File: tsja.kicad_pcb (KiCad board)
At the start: 4 copper layers, 95 x 86 mm, 114 parts, among them J1 QWIIC, J10 E-Paper, J2 Micro_SD_Card, J3 SAO, J4 EXT, J6 USB-C, J9 Battery, M1 Vibration, Q1 AP2302B, Q2 AP2302B, Q3 AP2302B, Q4 AO3400 (A09T), Q5 AO3400 (A09T), SW6 SW_SPDT, T1 Select, T2 Start, T3 B, T4 A, T5 Cross, U1 74LVC1G17GW,125, U10 SY6280AAC, U11 SK6805, U12 SK6805, U13 SK6805, U14 SK6805, U15 SK6805, U2 MPR121QR2, U3 ESP32-WROVER-E, U4 SY8079AAC, U5 XT4054K421MR-G, U6 SY6280AAC, U7 CH340K, U8 SK6805, U9 SY6280AAC

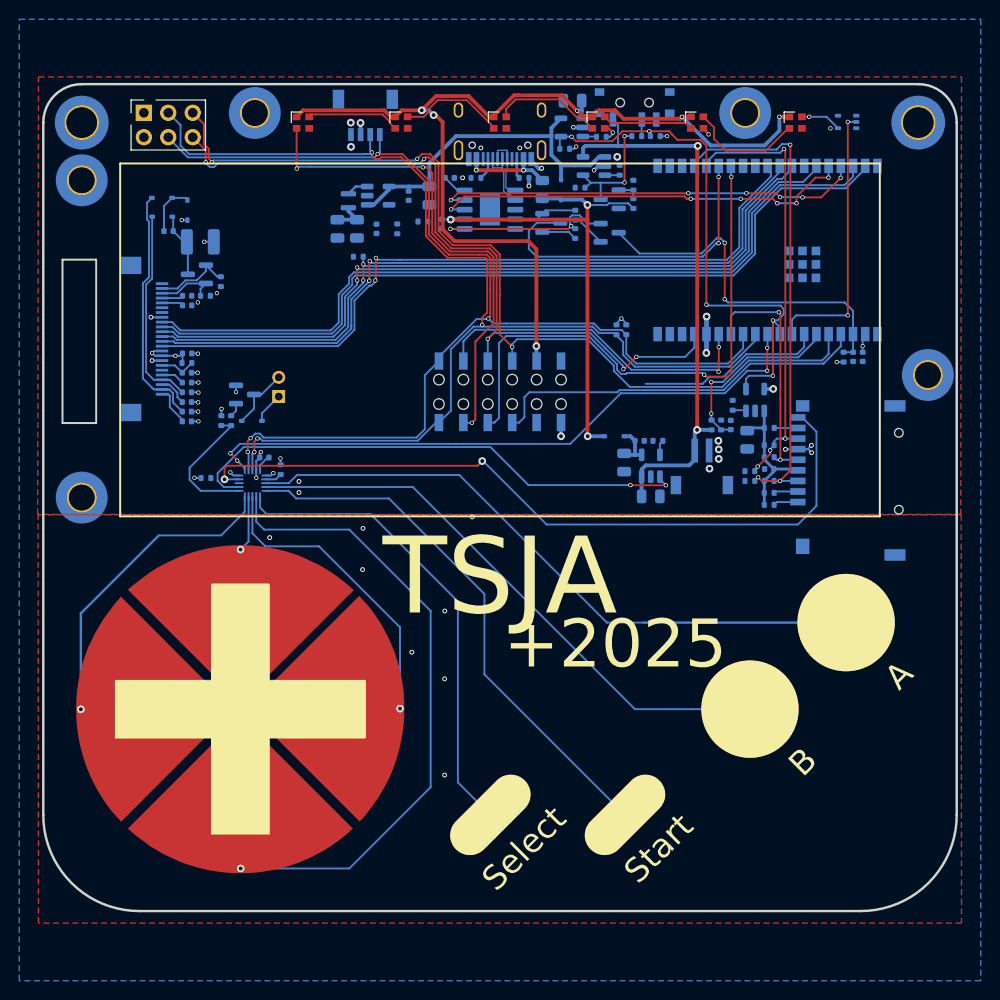
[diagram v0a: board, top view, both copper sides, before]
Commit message: Use DC/DC from WHY badge
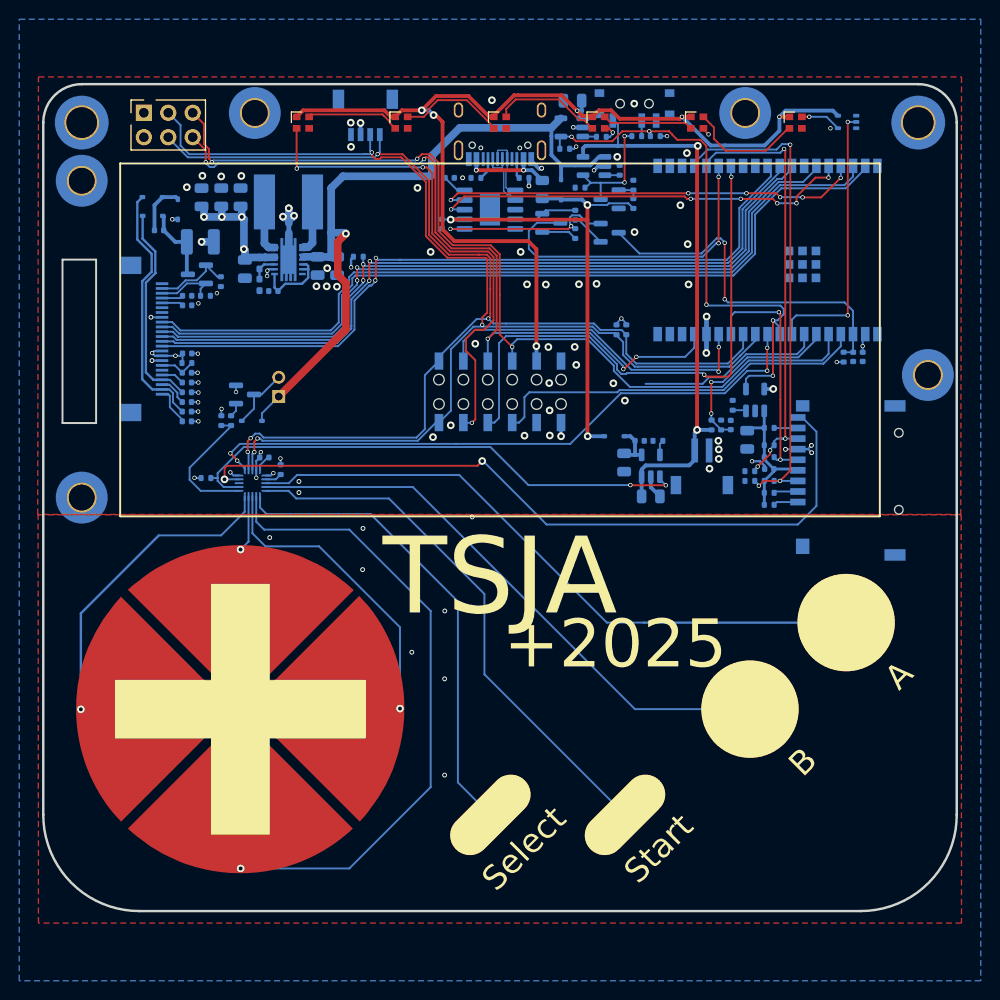
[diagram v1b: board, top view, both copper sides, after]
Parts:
- removed R23: 10k, Resistor_SMD:R_0402_1005Metric
- removed R24: 45.3k, Resistor_SMD:R_0402_1005Metric
- added C28: 10u, Capacitor_SMD:C_0805_2012Metric, B.Cu at (-19.0, -24.3)
- added C29: 100n, Capacitor_SMD:C_0402_1005Metric, B.Cu at (-23.6, -21.7)
- added JP1: ~, NetTie:NetTie-2_SMD_Pad0.5mm, B.Cu at (-22.0, -28.3)
- added R11: 1M, Resistor_SMD:R_0402_1005Metric_Pad0.72x0.64mm_HandSolder, B.Cu at (-25.0, -24.6)
- added R12: 180k, Resistor_SMD:R_0402_1005Metric_Pad0.72x0.64mm_HandSolder, B.Cu at (-25.0, -22.4)
- C10: value 22u -> 10u
- C4: value 100n -> 22u; footprint Capacitor_SMD:C_0402_1005Metric -> Capacitor_SMD:C_0805_2012Metric
- C7: value 22p -> 22u; footprint Capacitor_SMD:C_0402_1005Metric -> Capacitor_SMD:C_0805_2012Metric
- L1: value 2.2u -> CMLW6028S1R5MST; footprint library:Inductor_MSC20FC -> library:IND-SMD_L6.0-W6.0
- U4: value SY8079AAC -> TPS63020DSJR; footprint library:SOT-23-5 -> library:VSON-14_L4.0-W3.0-P0.50-BL-EP_TI_DSJ
- moved C5 19.6 mm to (-27.0, -31.5), turned to 90 degrees
- moved C4 18.7 mm to (-26.5, -24.0)
- moved C9 16.5 mm to (-31.0, -31.5), turned to 90 degrees
- moved C7 16.5 mm to (-29.0, -31.5)
- moved U4 11.5 mm to (-22.0, -25.0), turned to 90 degrees
- moved L1 6.24 mm to (-22.0, -31.0), turned to 0 degrees
- moved C10 3.87 mm to (-16.9, -24.3)
- moved C13 0.99 mm to (-35.5, -28.0)
- moved D25 0.99 mm to (-33.5, -30.2)
- moved D26 0.99 mm to (-36.1, -31.5)
- moved D27 0.99 mm to (-36.1, -29.5)
- moved SW6 0.11 mm to (14.0, -40.9)
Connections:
- C10 pad 1: +3.3V -> VIN
- C4 pad 1: VIN -> +3.3V
- C5 pad 1: VIN -> +3.3V
- C7 pad 2: /Power management/FB33 -> GND
- L1 pad 1: +3.3V -> Net-(L1-Pad1)
- L1 pad 2: /Power management/SW33 -> Net-(L1-Pad2)
- U4 pad 1: VIN -> Net-(U4-EN)
- U4 pad 3: /Power management/SW33 -> Net-(U4-FB)
- U4 pad 4: VIN -> +3.3V
- U4 pad 5: /Power management/FB33 -> +3.3V
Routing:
- net VIN: track 39.1 -> 74.9 mm, vias 0 -> 1
- net +3.3V: track 19.9 -> 32.9 mm, vias 11 -> 16
- net GND: track 30.7 -> 39.2 mm, vias 52 -> 92
- net Net-(U4-EN): track 0.00 -> 8.12 mm
- net VLED: track 99.0 -> 105.5 mm
- net Net-(L1-Pad1): track 0.00 -> 5.57 mm
- net Net-(L1-Pad2): track 0.00 -> 5.45 mm
- net Net-(U4-FB): track 0.00 -> 2.81 mm
- net GNDPWR: track 0.00 -> 2.79 mm
- net /Power management/SW33: track 2.27 -> 0.00 mm
- net LED_OUT: track 51.5 -> 52.8 mm
- net Net-(D27-A): track 6.84 -> 8.01 mm
- net /E-Paper/PREVGL: track 25.4 -> 26.3 mm
- net /E-Paper/PREVGH: track 21.1 -> 21.9 mm
- net CHRG: track 53.8 -> 54.5 mm

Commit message: Small fixes
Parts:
- H2: footprint MountingHole:MountingHole_3.2mm_M3_DIN965_Pad_TopOnly -> MountingHole:MountingHole_3.2mm_M3_DIN965
- H5: footprint MountingHole:MountingHole_2.7mm_M2.5_Pad_TopOnly -> MountingHole:MountingHole_2.7mm_M2.5_DIN965
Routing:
- net E4: track 39.9 -> 41.8 mm
- net VBUS: track 52.4 -> 53.4 mm
- net TOUCH_INT: track 65.5 -> 66.4 mm
- net GND: vias 92 -> 97

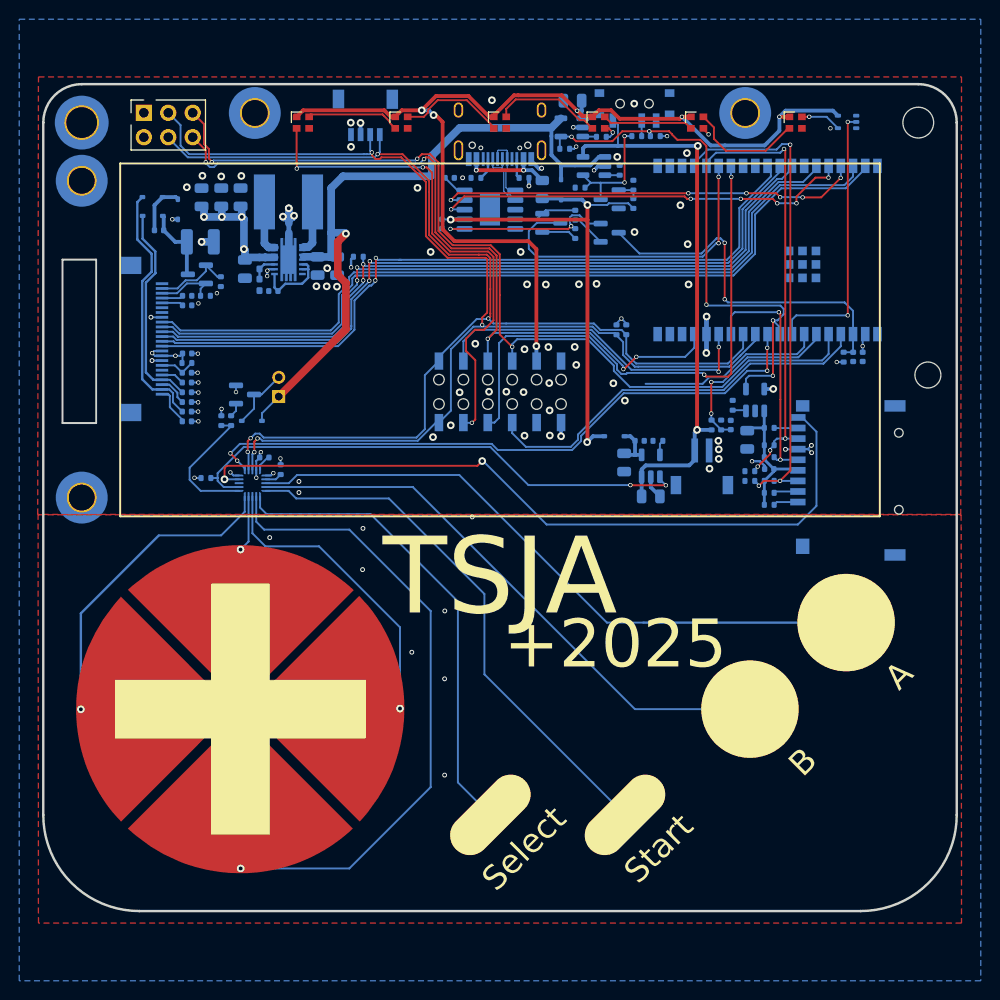
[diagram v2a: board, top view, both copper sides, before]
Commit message: Fix some routing issues, add GND vias, add capacitor for M1, add spacing between vias for ground to pour inbetween.
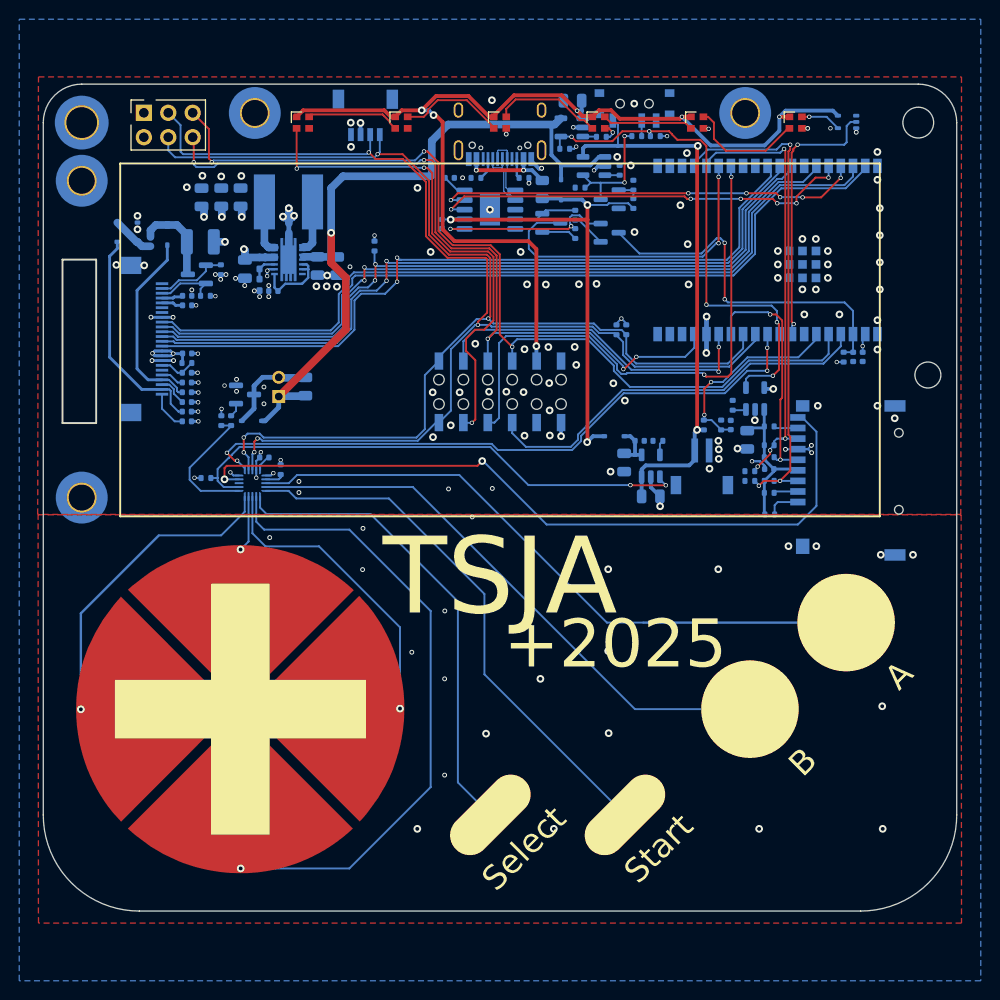
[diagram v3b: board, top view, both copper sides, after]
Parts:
- added C30: 22u, Capacitor_SMD:C_0805_2012Metric, B.Cu at (-20.2, -11.8)
- moved D25 5.43 mm to (-38.8, -28.9), turned to 180 degrees
- moved D26 5.33 mm to (-38.8, -26.9)
- moved D27 2.51 mm to (-34.6, -27.6), turned to 90 degrees
- moved R14 2.02 mm to (-13.1, -26.4), turned to -90 degrees
- moved C13 1.48 mm to (-36.4, -26.9), turned to 90 degrees
- moved R35 1.24 mm to (-29.0, -23.9)
- moved R17 1.00 mm to (28.1, 1.50)
- moved R31 0.80 mm to (21.2, -7.80)
- moved R22 0.15 mm to (28.0, -7.65)
- moved U9 0.15 mm to (26.5, -10.6)
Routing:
- net unconnected-(U3-GPIO35/ADC1_CH7-Pad7): track 19.4 -> 0.00 mm
- net +3.3V: track 32.9 -> 25.3 mm
- net VIN: track 74.9 -> 78.6 mm
- net /E-Paper/PREVGL: track 26.3 -> 23.0 mm
- net Net-(D21-A): track 6.58 -> 9.76 mm
- net PWR_EN: track 56.5 -> 54.4 mm
- net /E-Paper/PREVGH: track 21.9 -> 20.1 mm
- net VBATT: track 59.1 -> 57.3 mm
- net I2C_SCL: track 119.7 -> 120.8 mm
- net Net-(D25-A): track 5.49 -> 4.47 mm
- net Net-(J2-DAT2): track 2.59 -> 3.51 mm
- net Net-(U7-V3): track 2.57 -> 1.85 mm
- net Net-(SW6-B): track 1.95 -> 1.27 mm
- net /USB_P: track 6.88 -> 6.20 mm
- net SD_DET: track 78.6 -> 78.0 mm
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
